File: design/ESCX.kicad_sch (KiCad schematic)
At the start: 7 parts, among them J1 SWD

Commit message: Correccion de errores
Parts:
- J1: footprint Connector_JST:JST_XH_B5B-XH-AM_1x05_P2.50mm_Vertical -> Connector_PinHeader_2.54mm:PinHeader_1x05_P2.54mm_Vertical; Manufacturer JST -> Hanbo Electronic; Manufacturer Product Number  B5B-XH-A -> HB-PH3-25415PB2GOP
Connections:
- net +3.3V: now also J1.1 (Pin_1); no longer J1.5 (Pin_5)
- net MCU/NRST: now also J1.5 (Pin_5); no longer J1.1 (Pin_1)
- net MCU/SWCLK: now also J1.2 (Pin_2); no longer J1.4 (Pin_4)
- net MCU/SWDIO: now also J1.4 (Pin_4); no longer J1.2 (Pin_2)
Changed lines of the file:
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@@
 	(wire
 		(pts
-			(xy 95.25 123.19) (xy 73.66 123.19)
+			(xy 95.25 123.19) (xy 71.12 123.19)
 		)
 		(stroke
@@
 	(wire
 		(pts
-			(xy 73.66 130.81) (xy 95.25 130.81)
+			(xy 71.12 130.81) (xy 95.25 130.81)
 		)
 		(stroke
@@
 	(wire
 		(pts
-			(xy 73.66 128.27) (xy 95.25 128.27)
+			(xy 71.12 128.27) (xy 95.25 128.27)
 		)
 		(stroke
@@
 	(wire
 		(pts
+			(xy 71.12 125.73) (xy 73.66 125.73)
+		)
+		(stroke
+			(width 0)
+			(type default)
+		)
+	)
+	(wire
+		(pts
 			(xy 151.13 36.83) (xy 166.37 36.83)
 		)
@@
 		)
 	)
-	(symbol
-		(lib_id "Connector_Generic:Conn_01x05")
-		(at 68.58 125.73 180)
-		(unit 1)
-		(exclude_from_sim no)
-		(in_bom yes)
-		(on_board yes)
-		(dnp no)
-		(fields_autoplaced yes)
-		(property "Reference" "J1"
-			(at 68.58 114.3 0)
-			(effects
-				(font
-					(size 1.27 1.27)
-				)
-			)
-		)
-		(property "Value" "SWD"
-			(at 68.58 116.84 0)
-			(effects
-				(font
-					(size 1.27 1.27)
-				)
-			)
-		)
-		(property "Footprint" "Connector_JST:JST_XH_B5B-XH-AM_1x05_P2.50mm_Vertical"
-			(at 68.58 125.73 0)
-			(effects
-				(font
-					(size 1.27 1.27)
-				)
-				(hide yes)
-			)
-		)
-		(property "Datasheet" "~"
-			(at 68.58 125.73 0)
-			(effects
-				(font
-					(size 1.27 1.27)
-				)
-				(hide yes)
-			)
-		)
-		(property "Description" "5P"
-			(at 68.58 125.73 0)
-			(effects
-				(font
-					(size 1.27 1.27)
-				)
-				(hide yes)
-			)
-		)
-		(property "Availability" ""
-			(at 68.58 125.73 0)
-			(effects
-				(font
-					(size 1.27 1.27)
-				)
-				(hide yes)
-			)
-		)
-		(property "Check_prices" ""
-			(at 68.58 125.73 0)
-			(effects
-				(font
-					(size 1.27 1.27)
-				)
-				(hide yes)
-			)
-		)
-		(property "Description_1" ""
-			(at 68.58 125.73 0)
-			(effects
-				(font
-					(size 1.27 1.27)
-				)
-				(hide yes)
-			)
-		)
-		(property "MANUFACTURER" ""
-			(at 68.58 125.73 0)
-			(effects
-				(font
-					(size 1.27 1.27)
-				)
-				(hide yes)
-			)
-		)
-		(property "MF" ""
-			(at 68.58 125.73 0)
-			(effects
-				(font
-					(size 1.27 1.27)
-				)
-				(hide yes)
-			)
-		)
-		(property "MP" ""
-			(at 68.58 125.73 0)
-			(effects
-				(font
-					(size 1.27 1.27)
-				)
-				(hide yes)
-			)
-		)
-		(property "Package" ""
-			(at 68.58 125.73 0)
-			(effects
-				(font
-					(size 1.27 1.27)
-				)
-				(hide yes)
-			)
-		)
-		(property "Price" ""
-			(at 68.58 125.73 0)
-			(effects
-				(font
-					(size 1.27 1.27)
-				)
-				(hide yes)
-			)
-		)
-		(property "Purchase-URL" ""
-			(at 68.58 125.73 0)
-			(effects
-				(font
-					(size 1.27 1.27)
-				)
-				(hide yes)
-			)
-		)
-		(property "STANDARD" ""
-			(at 68.58 125.73 0)
-			(effects
-				(font
-					(size 1.27 1.27)
-				)
-				(hide yes)
-			)
-		)
-		(property "SnapEDA_Link" ""
-			(at 68.58 125.73 0)
-			(effects
-				(font
-					(size 1.27 1.27)
-				)
-				(hide yes)
-			)
-		)
-		(property "Manufacturer" "JST"
-			(at 68.58 125.73 0)
-			(effects
-				(font
-					(size 1.27 1.27)
-				)
-				(hide yes)
-			)
-		)
-		(property "Manufacturer Product Number " "B5B-XH-A"
-			(at 68.58 125.73 0)
-			(effects
-				(font
-					(size 1.27 1.27)
-				)
-				(hide yes)
-			)
-		)
-		(pin "1"
-		)
-		(pin "2"
-		)
-		(pin "3"
-		)
-		(pin "4"
-		)
-		(pin "5"
-		)
-		(instances
-			(project "ESCX"
-				(path "/6389d757-a1bd-4c0a-9d55-6114b19cc67a"
-					(reference "J1")
-					(unit 1)
-				)
-			)
+	(wire
+		(pts
+			(xy 71.12 120.65) (xy 73.66 120.65)
+		)
+		(stroke
+			(width 0)
+			(type default)
 		)
 	)
@@
 					(unit 1)
 				)
+			)
+		)
+	)
+	(symbol
+		(lib_id "Connector_Generic:Conn_01x05")
+		(at 66.04 125.73 0)
+		(mirror y)
+		(unit 1)
+		(exclude_from_sim no)
+		(in_bom yes)
+		(on_board yes)
+		(dnp no)
+		(property "Reference" "J1"
+			(at 63.5 124.4599 0)
+			(effects
+				(font
+					(size 1.27 1.27)
+				)
+				(justify left)
+			)
+		)
+		(property "Value" "SWD"
+			(at 63.5 126.9999 0)
+			(effects
+				(font
+					(size 1.27 1.27)
+				)
+				(justify left)
+			)
+		)
+		(property "Footprint" "Connector_PinHeader_2.54mm:PinHeader_1x05_P2.54mm_Vertical"
+			(at 66.04 125.73 0)
+			(effects
+				(font
+					(size 1.27 1.27)
+				)
+				(hide yes)
+			)
+		)
+		(property "Datasheet" "~"
+			(at 66.04 125.73 0)
+			(effects
+				(font
+					(size 1.27 1.27)
+				)
+				(hide yes)
+			)
+		)
+		(property "Description" "5P"
+			(at 66.04 125.73 0)
+			(effects
+				(font
+					(size 1.27 1.27)
+				)
+				(hide yes)
+			)
+		)
+		(property "Availability" ""
+			(at 66.04 125.73 0)
+			(effects
+				(font
+					(size 1.27 1.27)
+				)
+				(hide yes)
+			)
+		)
+		(property "Check_prices" ""
+			(at 66.04 125.73 0)
+			(effects
+				(font
+					(size 1.27 1.27)
+				)
+				(hide yes)
+			)
+		)
+		(property "Description_1" ""
+			(at 66.04 125.73 0)
+			(effects
+				(font
+					(size 1.27 1.27)
+				)
+				(hide yes)
+			)
+		)
+		(property "MANUFACTURER" ""
+			(at 66.04 125.73 0)
+			(effects
+				(font
+					(size 1.27 1.27)
+				)
+				(hide yes)
+			)
+		)
+		(property "MF" ""
+			(at 66.04 125.73 0)
+			(effects
+				(font
+					(size 1.27 1.27)
+				)
+				(hide yes)
+			)
+		)
+		(property "MP" ""
+			(at 66.04 125.73 0)
+			(effects
+				(font
+					(size 1.27 1.27)
+				)
+				(hide yes)
+			)
+		)
+		(property "Package" ""
+			(at 66.04 125.73 0)
+			(effects
+				(font
+					(size 1.27 1.27)
+				)
+				(hide yes)
+			)
+		)
+		(property "Price" ""
+			(at 66.04 125.73 0)
+			(effects
+				(font
+					(size 1.27 1.27)
+				)
+				(hide yes)
+			)
+		)
+		(property "Purchase-URL" ""
+			(at 66.04 125.73 0)
+			(effects
+				(font
+					(size 1.27 1.27)
+				)
+				(hide yes)
+			)
+		)
+		(property "STANDARD" ""
+			(at 66.04 125.73 0)
+			(effects
+				(font
+					(size 1.27 1.27)
+				)
+				(hide yes)
+			)
+		)
+		(property "SnapEDA_Link" ""
+			(at 66.04 125.73 0)
+			(effects
+				(font
+					(size 1.27 1.27)
+				)
+				(hide yes)
+			)
+		)
+		(property "Manufacturer" " Hanbo Electronic"
+			(at 66.04 125.73 0)
+			(effects
+				(font
+					(size 1.27 1.27)
+				)
+				(hide yes)
+			)
+		)
+		(property "Manufacturer Product Number " "HB-PH3-25415PB2GOP"
+			(at 66.04 125.73 0)
+			(effects
+				(font
+					(size 1.27 1.27)
+				)
+				(hide yes)
+			)
+		)
+		(pin "1"
+		)
+		(pin "2"
+		)
+		(pin "3"
+		)
+		(pin "4"
+		)
+		(pin "5"
+		)
+		(instances
+			(project "ESCX"
+				(path "/6389d757-a1bd-4c0a-9d55-6114b19cc67a"
+					(reference "J1")
+					(unit 1)
+				)

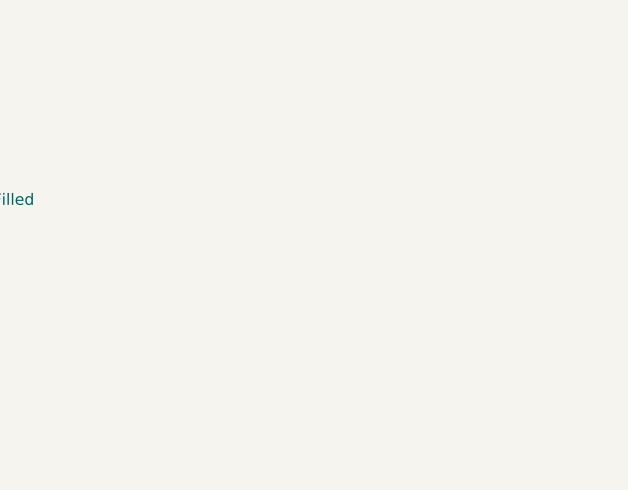
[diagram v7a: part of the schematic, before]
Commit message: Arreglos y cambios
Cambios en ruteos, dimensión de la placa, tamaño de las vías, parámetros de diseño jlcpb (constraints). Agregado de pad térmico de transistores, duplicado de capa inferior y superior para mejor disipación.
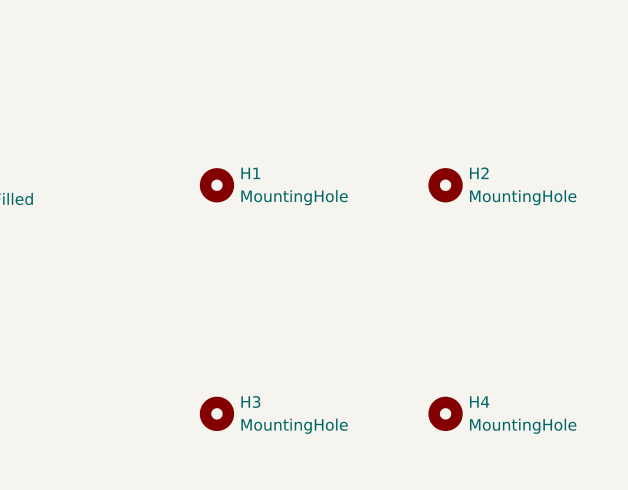
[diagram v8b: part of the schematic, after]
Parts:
- added H1, H2, H3, H4: MountingHole, MountingHole:MountingHole_2.7mm_M2.5, symbol Mechanical:MountingHole
